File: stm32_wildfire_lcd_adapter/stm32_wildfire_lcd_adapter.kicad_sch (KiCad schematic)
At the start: 2 parts, among them J1 Wildfire_40P_LCD, J2 STM32_40_LCD

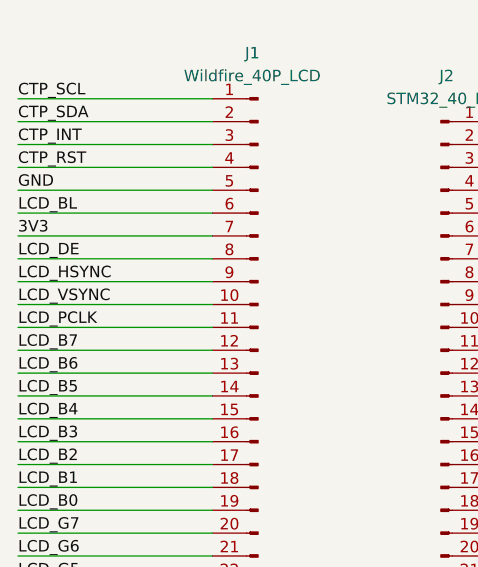
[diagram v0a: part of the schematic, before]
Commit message: fixing pinout error from wrong manual
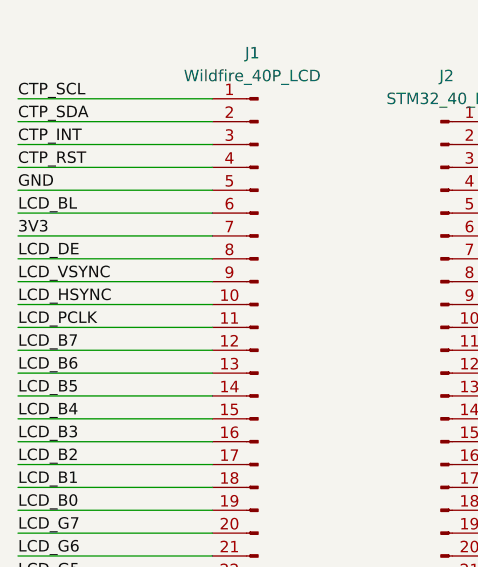
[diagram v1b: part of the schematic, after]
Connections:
- net LCD_HSYNC: now also J1.10 (Pin_10); no longer J1.9 (Pin_9)
- net LCD_VSYNC: now also J1.9 (Pin_9); no longer J1.10 (Pin_10)
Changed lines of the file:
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@@
 	)
 	(label "LCD_HSYNC"
-		(at 93.98 64.77 0)
+		(at 93.98 67.31 0)
 		(effects
 			(font
@@
 	)
 	(label "LCD_VSYNC"
-		(at 93.98 67.31 0)
+		(at 93.98 64.77 0)
 		(effects
 			(font

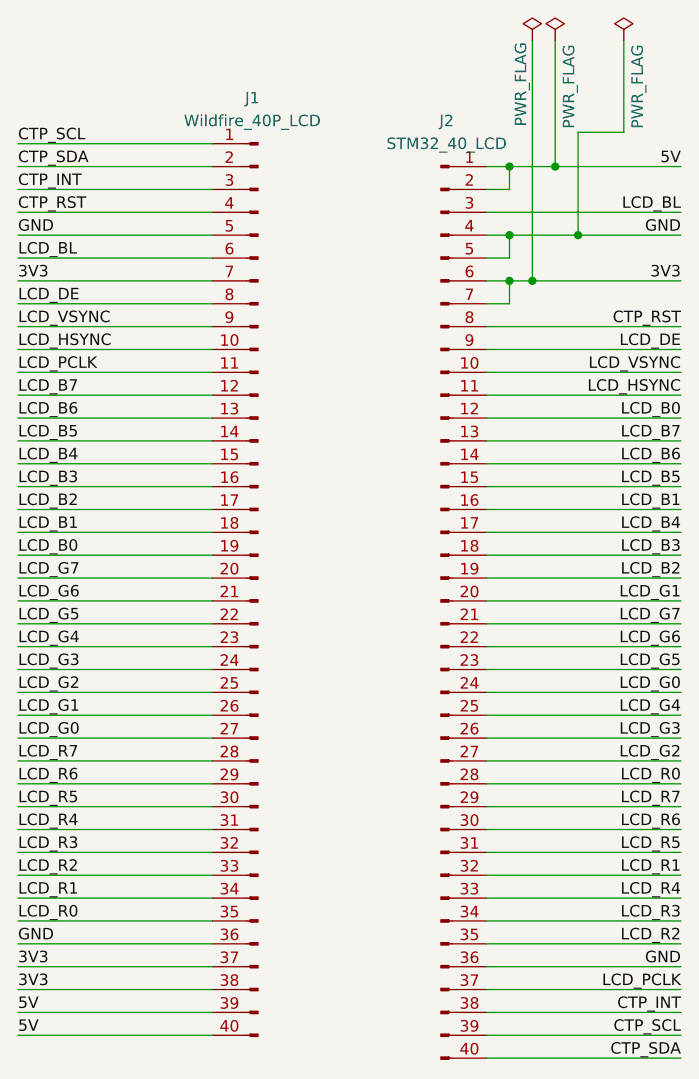
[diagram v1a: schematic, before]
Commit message: fixing fucking flipped fpc connector. how stupid of me!
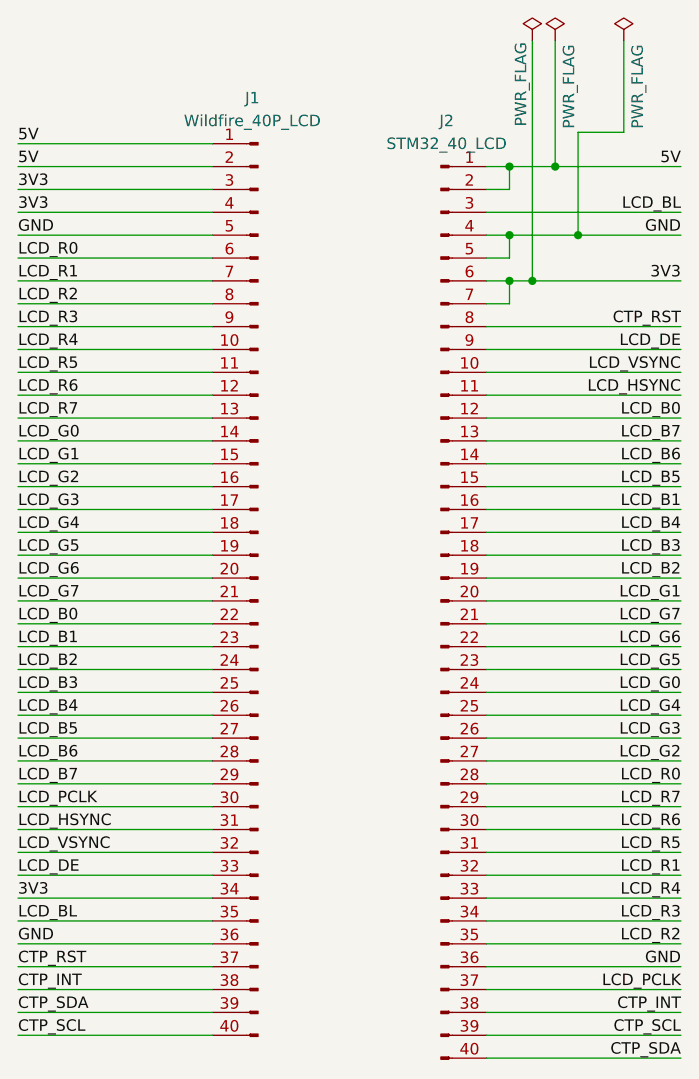
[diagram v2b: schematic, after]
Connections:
- net 3V3: now also J1.3 (Pin_3), J1.34 (Pin_34), J1.4 (Pin_4); no longer J1.37 (Pin_37), J1.38 (Pin_38), J1.7 (Pin_7)
- net 5V: now also J1.1 (Pin_1), J1.2 (Pin_2); no longer J1.39 (Pin_39), J1.40 (Pin_40)
- net CTP_INT: now also J1.38 (Pin_38); no longer J1.3 (Pin_3)
- net CTP_RST: now also J1.37 (Pin_37); no longer J1.4 (Pin_4)
- net CTP_SCL: now also J1.40 (Pin_40); no longer J1.1 (Pin_1)
- net CTP_SDA: now also J1.39 (Pin_39); no longer J1.2 (Pin_2)
- net LCD_B0: now also J1.22 (Pin_22); no longer J1.19 (Pin_19)
- net LCD_B1: now also J1.23 (Pin_23); no longer J1.18 (Pin_18)
- net LCD_B2: now also J1.24 (Pin_24); no longer J1.17 (Pin_17)
- net LCD_B3: now also J1.25 (Pin_25); no longer J1.16 (Pin_16)
- net LCD_B4: now also J1.26 (Pin_26); no longer J1.15 (Pin_15)
- net LCD_B5: now also J1.27 (Pin_27); no longer J1.14 (Pin_14)
- net LCD_B6: now also J1.28 (Pin_28); no longer J1.13 (Pin_13)
- net LCD_B7: now also J1.29 (Pin_29); no longer J1.12 (Pin_12)
- net LCD_BL: now also J1.35 (Pin_35); no longer J1.6 (Pin_6)
- net LCD_DE: now also J1.33 (Pin_33); no longer J1.8 (Pin_8)
- net LCD_G0: now also J1.14 (Pin_14); no longer J1.27 (Pin_27)
- net LCD_G1: now also J1.15 (Pin_15); no longer J1.26 (Pin_26)
- net LCD_G2: now also J1.16 (Pin_16); no longer J1.25 (Pin_25)
- net LCD_G3: now also J1.17 (Pin_17); no longer J1.24 (Pin_24)
- net LCD_G4: now also J1.18 (Pin_18); no longer J1.23 (Pin_23)
- net LCD_G5: now also J1.19 (Pin_19); no longer J1.22 (Pin_22)
- net LCD_G6: now also J1.20 (Pin_20); no longer J1.21 (Pin_21)
- net LCD_G7: now also J1.21 (Pin_21); no longer J1.20 (Pin_20)
- net LCD_HSYNC: now also J1.31 (Pin_31); no longer J1.10 (Pin_10)
- net LCD_PCLK: now also J1.30 (Pin_30); no longer J1.11 (Pin_11)
- net LCD_R0: now also J1.6 (Pin_6); no longer J1.35 (Pin_35)
- net LCD_R1: now also J1.7 (Pin_7); no longer J1.34 (Pin_34)
- net LCD_R2: now also J1.8 (Pin_8); no longer J1.33 (Pin_33)
- net LCD_R3: now also J1.9 (Pin_9); no longer J1.32 (Pin_32)
- net LCD_R4: now also J1.10 (Pin_10); no longer J1.31 (Pin_31)
- net LCD_R5: now also J1.11 (Pin_11); no longer J1.30 (Pin_30)
- net LCD_R6: now also J1.12 (Pin_12); no longer J1.29 (Pin_29)
- net LCD_R7: now also J1.13 (Pin_13); no longer J1.28 (Pin_28)
- net LCD_VSYNC: now also J1.32 (Pin_32); no longer J1.9 (Pin_9)
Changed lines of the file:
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@@
 		)
 	)
-	(label "LCD_G2"
+	(label "LCD_B3"
 		(at 93.98 105.41 0)
 		(effects
@@
 		)
 	)
-	(label "LCD_B4"
+	(label "LCD_G1"
 		(at 93.98 80.01 0)
 		(effects
@@
 		)
 	)
-	(label "LCD_R5"
+	(label "LCD_PCLK"
 		(at 93.98 118.11 0)
 		(effects
@@
 		)
 	)
-	(label "LCD_BL"
+	(label "LCD_R0"
 		(at 93.98 57.15 0)
 		(effects
@@
 		)
 	)
-	(label "CTP_SCL"
+	(label "5V"
 		(at 93.98 44.45 0)
 		(effects
@@
 		)
 	)
-	(label "3V3"
+	(label "CTP_RST"
 		(at 93.98 135.89 0)
 		(effects
@@
 		)
 	)
-	(label "LCD_G5"
+	(label "LCD_B0"
 		(at 93.98 97.79 0)
 		(effects
@@
 		)
 	)
-	(label "CTP_INT"
+	(label "3V3"
 		(at 93.98 49.53 0)
 		(effects
@@
 		)
 	)
-	(label "3V3"
+	(label "CTP_INT"
 		(at 93.98 138.43 0)
 		(effects
@@
 		)
 	)
-	(label "LCD_R2"
+	(label "LCD_DE"
 		(at 93.98 125.73 0)
 		(effects
@@
 		)
 	)
-	(label "LCD_G3"
+	(label "LCD_B2"
 		(at 93.98 102.87 0)
 		(effects
@@
 		)
 	)
-	(label "LCD_G0"
+	(label "LCD_B5"
 		(at 93.98 110.49 0)
 		(effects
@@
 		)
 	)
-	(label "LCD_R6"
+	(label "LCD_B7"
 		(at 93.98 115.57 0)
 		(effects
@@
 		)
 	)
-	(label "LCD_G1"
+	(label "LCD_B4"
 		(at 93.98 107.95 0)
 		(effects
@@
 		)
 	)
-	(label "LCD_G6"
+	(label "LCD_G7"
 		(at 93.98 95.25 0)
 		(effects
@@
 		)
 	)
-	(label "LCD_G4"
+	(label "LCD_B1"
 		(at 93.98 100.33 0)
 		(effects
@@
 		)
 	)
-	(label "LCD_B1"
+	(label "LCD_G4"
 		(at 93.98 87.63 0)
 		(effects
@@
 		)
 	)
-	(label "3V3"
+	(label "LCD_R1"
 		(at 93.98 59.69 0)
 		(effects
@@
 		)
 	)
-	(label "LCD_B5"
+	(label "LCD_G0"
 		(at 93.98 77.47 0)
 		(effects
@@
 		)
 	)
-	(label "LCD_PCLK"
+	(label "LCD_R5"
 		(at 93.98 69.85 0)
 		(effects
@@
 		)
 	)
-	(label "LCD_R0"
+	(label "LCD_BL"
 		(at 93.98 130.81 0)
 		(effects
@@
 		)
 	)
+	(label "LCD_R7"
+		(at 93.98 74.93 0)
+		(effects
+			(font
+				(size 1.27 1.27)
+			)
+			(justify left bottom)
+		)
+	)
 	(label "LCD_B6"
-		(at 93.98 74.93 0)
-		(effects
-			(font
-				(size 1.27 1.27)
-			)
-			(justify left bottom)
-		)
-	)
-	(label "LCD_R7"
 		(at 93.98 113.03 0)
 		(effects
@@
 		)
 	)
-	(label "LCD_G7"
+	(label "LCD_G6"
 		(at 93.98 92.71 0)
 		(effects
@@
 		)
 	)
-	(label "LCD_R3"
+	(label "LCD_VSYNC"
 		(at 93.98 123.19 0)
 		(effects
@@
 		)
 	)
-	(label "LCD_HSYNC"
+	(label "LCD_R4"
 		(at 93.98 67.31 0)
 		(effects
@@
 		)
 	)
-	(label "LCD_VSYNC"
+	(label "LCD_R3"
 		(at 93.98 64.77 0)
 		(effects
@@
 		)
 	)
-	(label "LCD_B7"
+	(label "LCD_R6"
 		(at 93.98 72.39 0)
 		(effects
@@
 		)
 	)
-	(label "LCD_R4"
+	(label "LCD_HSYNC"
 		(at 93.98 120.65 0)
 		(effects
@@
 		)
 	)
-	(label "LCD_B0"
+	(label "LCD_G5"
 		(at 93.98 90.17 0)
 		(effects
@@
 		)
 	)
-	(label "5V"
+	(label "CTP_SDA"
 		(at 93.98 140.97 0)
 		(effects
@@
 		)
 	)
-	(label "LCD_B3"
+	(label "LCD_G2"
 		(at 93.98 82.55 0)
 		(effects
@@
 		)
 	)
-	(label "CTP_RST"
+	(label "3V3"
 		(at 93.98 52.07 0)
 		(effects
@@
 		)
 	)
-	(label "LCD_R1"
+	(label "3V3"
 		(at 93.98 128.27 0)
 		(effects
@@
 		)
 	)
-	(label "LCD_B2"
+	(label "LCD_G3"
 		(at 93.98 85.09 0)
 		(effects
@@
 		)
 	)
-	(label "5V"
+	(label "CTP_SCL"
 		(at 93.98 143.51 0)
 		(effects
@@
 		)
 	)
-	(label "LCD_DE"
+	(label "LCD_R2"
 		(at 93.98 62.23 0)
 		(effects
@@
 		)
 	)
-	(label "CTP_SDA"
+	(label "5V"
 		(at 93.98 46.99 0)
 		(effects
